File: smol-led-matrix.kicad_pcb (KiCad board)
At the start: 4 copper layers, 20.4 x 20.4 mm, 226 parts, among them U1 STM32L431CBTx

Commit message: Place parts
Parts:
- added C1: 100nF, Capacitor_SMD:C_0402_1005Metric, F.Cu at (131.6, 118.8)
- added C2: 100nF, Capacitor_SMD:C_0402_1005Metric, F.Cu at (124.8, 115.7)
- added C3: 100nF, Capacitor_SMD:C_0402_1005Metric, F.Cu at (144.2, 102.6)
- added C4: 1uF, Capacitor_SMD:C_0402_1005Metric, F.Cu at (139.3, 99.8)
- added C5: 100nF, Capacitor_SMD:C_0402_1005Metric, F.Cu at (129.8, 118.8)
- added C6: 1uF, Capacitor_SMD:C_0402_1005Metric, F.Cu at (138.8, 111.2)
- added C7: 1uF, Capacitor_SMD:C_0402_1005Metric, F.Cu at (140.5, 111.2)
- added C8: 100nF, Capacitor_SMD:C_0402_1005Metric, F.Cu at (126.1, 109.3)
- added C9: 100nF, Capacitor_SMD:C_0402_1005Metric, F.Cu at (134.3, 109.3)
- added D226: 1N4148, Diode_SMD:D_SOD-323F, F.Cu at (140.3, 101.9)
- added D227: LED, LED_SMD:LED_0402_1005Metric, F.Cu at (140.8, 99.6)
- added J1: USB_C_Receptacle_USB2.0, Connector_USB:USB_C_Receptacle_Palconn_UTC16-G, F.Cu at (129.4, 103.2)
- added J2: TagConnect_TC2030_SWD, Connector:Tag-Connect_TC2030-IDC-NL_2x03_P1.27mm_Vertical, F.Cu at (137.7, 117.3)
- added Q1: FS8205, Package_TO_SOT_SMD:SOT-23-6, F.Cu at (139.2, 105.3)
- added Q2: AO3401A, Package_TO_SOT_SMD:SOT-23, F.Cu at (139.6, 108.8)
- added R1: 5.1kR, Resistor_SMD:R_0402_1005Metric, F.Cu at (131.2, 107.3)
- added R2: 5.1kR, Resistor_SMD:R_0402_1005Metric, F.Cu at (127.1, 107.3)
- added R3: 27kR, Resistor_SMD:R_0402_1005Metric, F.Cu at (134.9, 102.9)
- added R4: 27kR, Resistor_SMD:R_0402_1005Metric, F.Cu at (136.7, 102.8)
- added R5: 27kR, Resistor_SMD:R_0402_1005Metric, F.Cu at (143.5, 107.7)
- added RN1: 1kR, Resistor_SMD:R_Array_Concave_4x0402, F.Cu at (136.2, 113.4)
- added RN2: 1kR, Resistor_SMD:R_Array_Concave_4x0402, F.Cu at (142.5, 102.5)
- added RN3: 1kR, Resistor_SMD:R_Array_Concave_4x0402, F.Cu at (136.9, 108.4)
- added RN4: 1kR, Resistor_SMD:R_Array_Concave_4x0402, F.Cu at (136.9, 110.9)
- added RN5: 1kR, Resistor_SMD:R_Array_Concave_4x0402, F.Cu at (136.0, 105.9)
- added SW1: SW_Push, Button_Switch_SMD:SW_Push_SPST_NO_Alps_SKRK, F.Cu at (142.9, 111.1)
- added SW2: SW_Push, Button_Switch_SMD:SW_Push_SPST_NO_Alps_SKRK, F.Cu at (142.9, 116.5)
- added TP1: BAT+, TestPoint:TestPoint_Pad_2.0x2.0mm, F.Cu at (125.6, 118.0)
- added TP2: BAT-, TestPoint:TestPoint_Pad_2.0x2.0mm, F.Cu at (143.4, 100.2)
- added U2: DW01+G, Package_TO_SOT_SMD:SOT-23-6, F.Cu at (142.8, 105.3)
- added U3: TP4054, Package_TO_SOT_SMD:TSOT-23-5, F.Cu at (136.6, 100.6)
- added U4: XC6206P332MR, Package_TO_SOT_SMD:SOT-23, F.Cu at (139.5, 113.5)
- U1: value STM32L431CBTx -> STM32L433CBTx
- moved U1 4.60 mm to (130.2, 113.4), turned to 90 degrees
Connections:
- net Net-(U1-Pad28) renamed /K15
- U1 pad 18: Net-(U1-Pad18) -> /K0
- U1 pad 19: Net-(U1-Pad19) -> /K1
- U1 pad 20: Net-(U1-Pad20) -> /K2
- U1 pad 21: Net-(U1-Pad21) -> /K10
- U1 pad 22: Net-(U1-Pad22) -> /K11
- U1 pad 23: Net-(U1-Pad23) -> GND
- U1 pad 24: Net-(U1-Pad24) -> +3V3
- U1 pad 25: Net-(U1-Pad25) -> /K12
- U1 pad 26: Net-(U1-Pad26) -> /K13
- U1 pad 27: Net-(U1-Pad27) -> /K14
- U1 pad 32: Net-(U1-Pad32) -> /D-
- U1 pad 33: Net-(U1-Pad33) -> /D+
- U1 pad 35: Net-(U1-Pad35) -> GND
- U1 pad 36: Net-(U1-Pad36) -> +3V3
- U1 pad 39: Net-(U1-Pad39) -> /K3
- U1 pad 40: Net-(U1-Pad40) -> /K4
- U1 pad 41: Net-(U1-Pad41) -> /K5
- U1 pad 42: Net-(U1-Pad42) -> /K6
- U1 pad 43: Net-(U1-Pad43) -> /K7
- U1 pad 45: Net-(U1-Pad45) -> /K8
- U1 pad 46: Net-(U1-Pad46) -> /K9
- U1 pad 47: Net-(U1-Pad47) -> GND
- U1 pad 48: Net-(U1-Pad48) -> +3V3
- U1 pad 7: Net-(U1-Pad7) -> /~RST
- U1 pad 8: Net-(U1-Pad8) -> GND
- U1 pad 9: Net-(U1-Pad9) -> +3V3
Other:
- board size 20.4 x 20.4 mm -> 45.8 x 20.4 mm

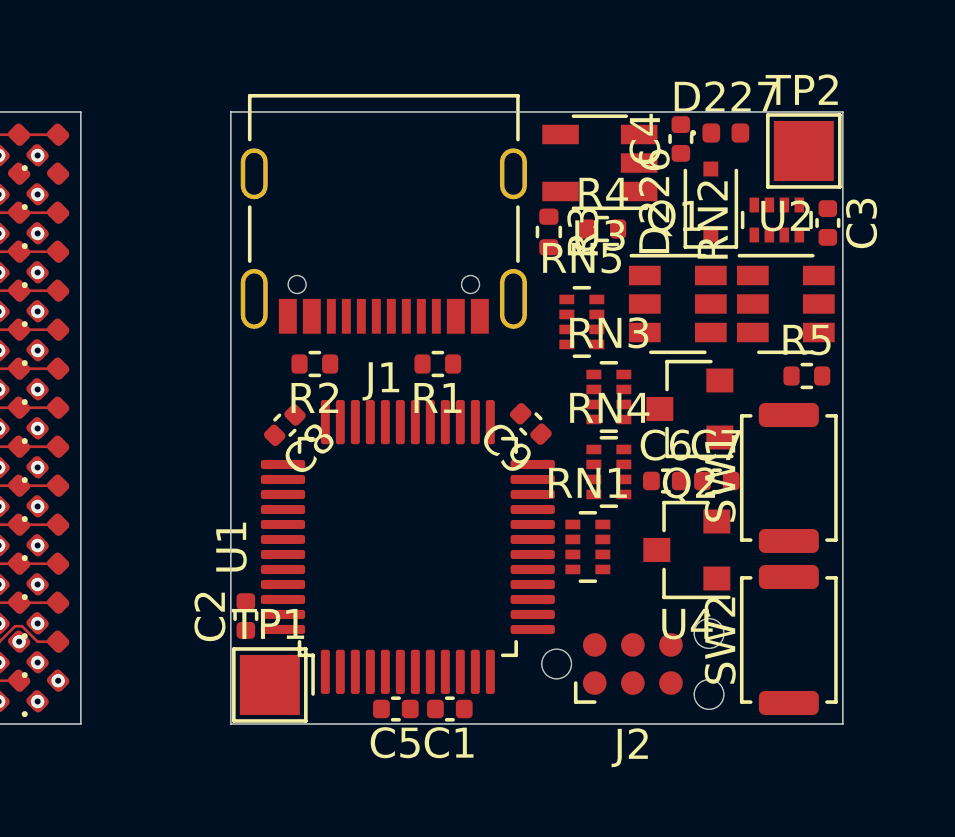
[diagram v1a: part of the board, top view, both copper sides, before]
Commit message: Hide designators
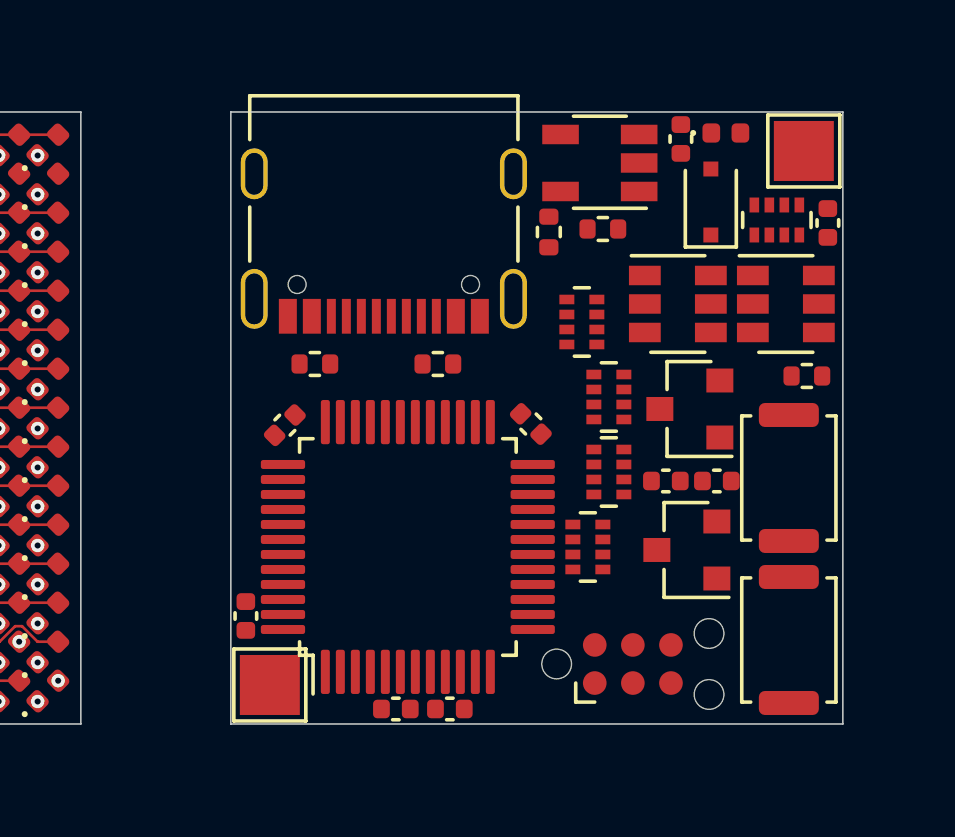
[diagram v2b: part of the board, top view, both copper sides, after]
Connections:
- net Net-(C3-Pad1) renamed /BAT-

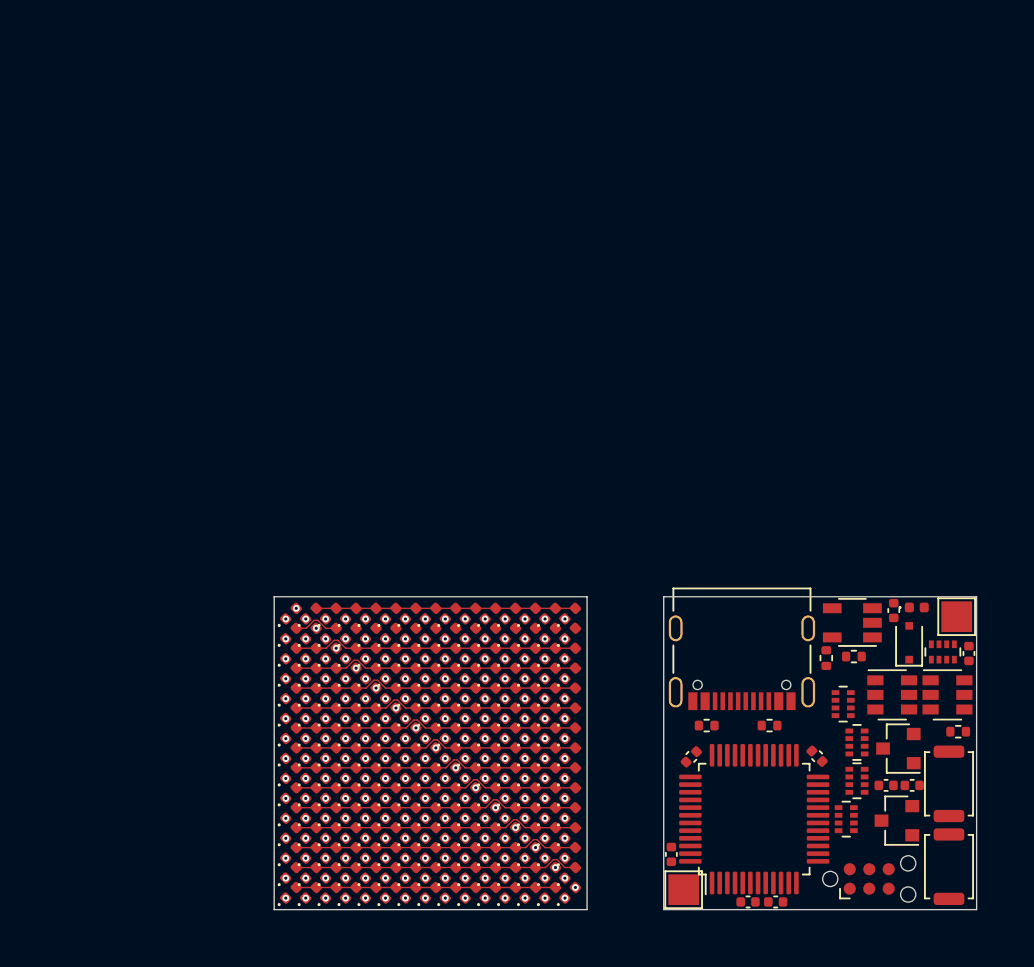
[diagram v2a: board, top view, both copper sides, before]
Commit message: Decide BGA ball placement
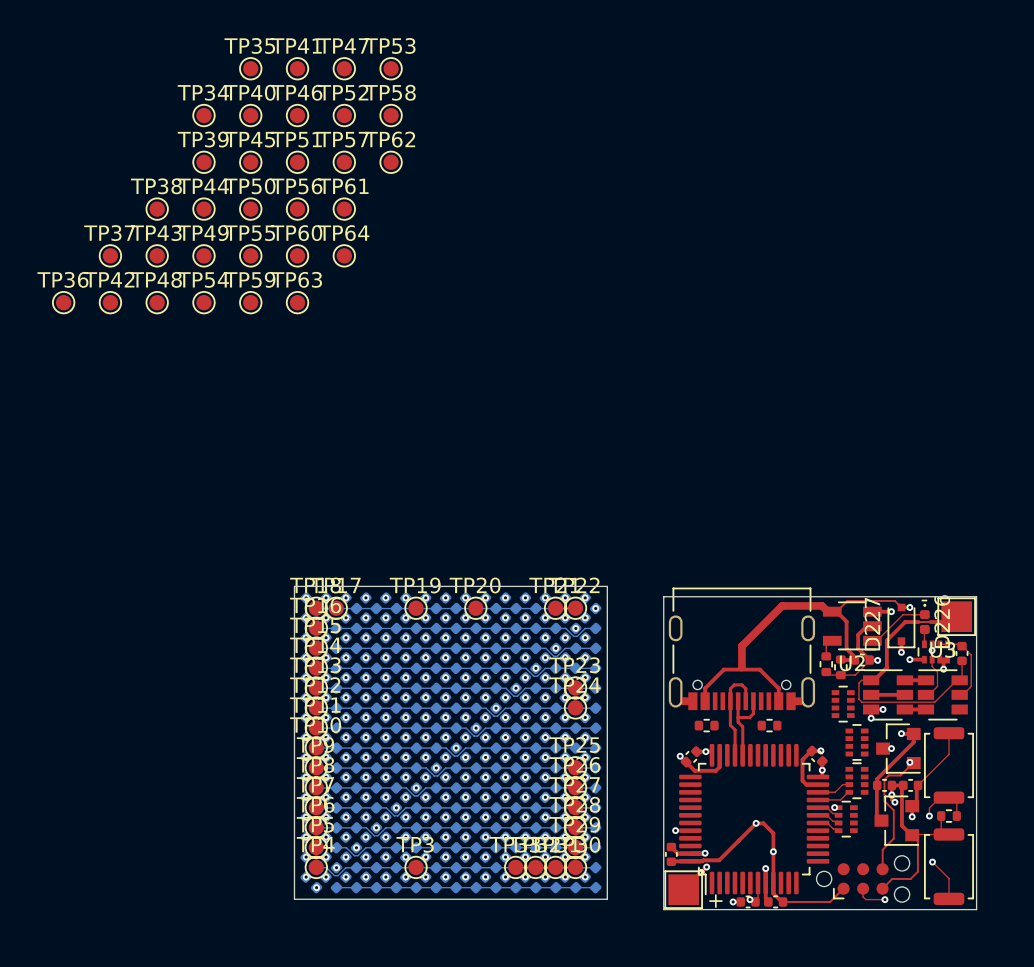
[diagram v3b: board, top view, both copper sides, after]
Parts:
- added TP10: TestPoint, TestPoint:TestPoint_Pad_D1.0mm, F.Cu at (101.7, 108.8)
- added TP11: TestPoint, TestPoint:TestPoint_Pad_D1.0mm, F.Cu at (101.7, 107.5)
- added TP12: TestPoint, TestPoint:TestPoint_Pad_D1.0mm, F.Cu at (101.7, 106.2)
- added TP13: TestPoint, TestPoint:TestPoint_Pad_D1.0mm, F.Cu at (101.7, 104.8)
- added TP14: TestPoint, TestPoint:TestPoint_Pad_D1.0mm, F.Cu at (101.7, 103.5)
- added TP15: TestPoint, TestPoint:TestPoint_Pad_D1.0mm, F.Cu at (101.7, 102.2)
- added TP16: TestPoint, TestPoint:TestPoint_Pad_D1.0mm, F.Cu at (101.7, 101.0)
- added TP17: TestPoint, TestPoint:TestPoint_Pad_D1.0mm, F.Cu at (103.0, 99.7)
- added TP18: TestPoint, TestPoint:TestPoint_Pad_D1.0mm, F.Cu at (101.7, 99.7)
- added TP19: TestPoint, TestPoint:TestPoint_Pad_D1.0mm, F.Cu at (108.2, 99.7)
- added TP20: TestPoint, TestPoint:TestPoint_Pad_D1.0mm, F.Cu at (112.0, 99.7)
- added TP21: TestPoint, TestPoint:TestPoint_Pad_D1.0mm, F.Cu at (117.2, 99.7)
- added TP22: TestPoint, TestPoint:TestPoint_Pad_D1.0mm, F.Cu at (118.5, 99.7)
- added TP23: TestPoint, TestPoint:TestPoint_Pad_D1.0mm, F.Cu at (118.5, 104.8)
- added TP24: TestPoint, TestPoint:TestPoint_Pad_D1.0mm, F.Cu at (118.5, 106.2)
- added TP25: TestPoint, TestPoint:TestPoint_Pad_D1.0mm, F.Cu at (118.5, 110.0)
- added TP26: TestPoint, TestPoint:TestPoint_Pad_D1.0mm, F.Cu at (118.5, 111.3)
- added TP27: TestPoint, TestPoint:TestPoint_Pad_D1.0mm, F.Cu at (118.5, 112.7)
- added TP28: TestPoint, TestPoint:TestPoint_Pad_D1.0mm, F.Cu at (118.5, 114.0)
- added TP29: TestPoint, TestPoint:TestPoint_Pad_D1.0mm, F.Cu at (118.5, 115.2)
- added TP3: TestPoint, TestPoint:TestPoint_Pad_D1.0mm, F.Cu at (108.2, 116.5)
- added TP30: TestPoint, TestPoint:TestPoint_Pad_D1.0mm, F.Cu at (118.5, 116.5)
- added TP31: TestPoint, TestPoint:TestPoint_Pad_D1.0mm, F.Cu at (117.2, 116.5)
- added TP32: TestPoint, TestPoint:TestPoint_Pad_D1.0mm, F.Cu at (116.0, 116.5)
- added TP33: TestPoint, TestPoint:TestPoint_Pad_D1.0mm, F.Cu at (114.7, 116.5)
- added TP34: TestPoint, TestPoint:TestPoint_Pad_D1.0mm, F.Cu at (94.3, 67.5)
- added TP35: TestPoint, TestPoint:TestPoint_Pad_D1.0mm, F.Cu at (97.4, 64.5)
- added TP36: TestPoint, TestPoint:TestPoint_Pad_D1.0mm, F.Cu at (85.2, 79.7)
- added TP37: TestPoint, TestPoint:TestPoint_Pad_D1.0mm, F.Cu at (88.2, 76.7)
- added TP38: TestPoint, TestPoint:TestPoint_Pad_D1.0mm, F.Cu at (91.3, 73.6)
- added TP39: TestPoint, TestPoint:TestPoint_Pad_D1.0mm, F.Cu at (94.3, 70.6)
- added TP4: TestPoint, TestPoint:TestPoint_Pad_D1.0mm, F.Cu at (101.7, 116.5)
- added TP40: TestPoint, TestPoint:TestPoint_Pad_D1.0mm, F.Cu at (97.4, 67.5)
- added TP41: TestPoint, TestPoint:TestPoint_Pad_D1.0mm, F.Cu at (100.4, 64.5)
- added TP42: TestPoint, TestPoint:TestPoint_Pad_D1.0mm, F.Cu at (88.2, 79.7)
- added TP43: TestPoint, TestPoint:TestPoint_Pad_D1.0mm, F.Cu at (91.3, 76.7)
- added TP44: TestPoint, TestPoint:TestPoint_Pad_D1.0mm, F.Cu at (94.3, 73.6)
- added TP45: TestPoint, TestPoint:TestPoint_Pad_D1.0mm, F.Cu at (97.4, 70.6)
- added TP46: TestPoint, TestPoint:TestPoint_Pad_D1.0mm, F.Cu at (100.4, 67.5)
- added TP47: TestPoint, TestPoint:TestPoint_Pad_D1.0mm, F.Cu at (103.5, 64.5)
- added TP48: TestPoint, TestPoint:TestPoint_Pad_D1.0mm, F.Cu at (91.3, 79.7)
- added TP49: TestPoint, TestPoint:TestPoint_Pad_D1.0mm, F.Cu at (94.3, 76.7)
- added TP5: TestPoint, TestPoint:TestPoint_Pad_D1.0mm, F.Cu at (101.7, 115.2)
- added TP50: TestPoint, TestPoint:TestPoint_Pad_D1.0mm, F.Cu at (97.4, 73.6)
- added TP51: TestPoint, TestPoint:TestPoint_Pad_D1.0mm, F.Cu at (100.4, 70.6)
- added TP52: TestPoint, TestPoint:TestPoint_Pad_D1.0mm, F.Cu at (103.5, 67.5)
- added TP53: TestPoint, TestPoint:TestPoint_Pad_D1.0mm, F.Cu at (106.5, 64.5)
- added TP54: TestPoint, TestPoint:TestPoint_Pad_D1.0mm, F.Cu at (94.3, 79.7)
- added TP55: TestPoint, TestPoint:TestPoint_Pad_D1.0mm, F.Cu at (97.4, 76.7)
- added TP56: TestPoint, TestPoint:TestPoint_Pad_D1.0mm, F.Cu at (100.4, 73.6)
- added TP57: TestPoint, TestPoint:TestPoint_Pad_D1.0mm, F.Cu at (103.5, 70.6)
- added TP58: TestPoint, TestPoint:TestPoint_Pad_D1.0mm, F.Cu at (106.5, 67.5)
- added TP59: TestPoint, TestPoint:TestPoint_Pad_D1.0mm, F.Cu at (97.4, 79.7)
- added TP6: TestPoint, TestPoint:TestPoint_Pad_D1.0mm, F.Cu at (101.7, 114.0)
- added TP60: TestPoint, TestPoint:TestPoint_Pad_D1.0mm, F.Cu at (100.4, 76.7)
- added TP61: TestPoint, TestPoint:TestPoint_Pad_D1.0mm, F.Cu at (103.5, 73.6)
- added TP62: TestPoint, TestPoint:TestPoint_Pad_D1.0mm, F.Cu at (106.5, 70.6)
- added TP63: TestPoint, TestPoint:TestPoint_Pad_D1.0mm, F.Cu at (100.4, 79.7)
- added TP64: TestPoint, TestPoint:TestPoint_Pad_D1.0mm, F.Cu at (103.5, 76.7)
- added TP7: TestPoint, TestPoint:TestPoint_Pad_D1.0mm, F.Cu at (101.7, 112.7)
- added TP8: TestPoint, TestPoint:TestPoint_Pad_D1.0mm, F.Cu at (101.7, 111.3)
- added TP9: TestPoint, TestPoint:TestPoint_Pad_D1.0mm, F.Cu at (101.7, 110.0)
- C3: value 100nF -> 1uF
- C4: value 1uF -> 100nF
- D1, D10, D100, D101, D102, D103, D104, D105, D106, D107, D108, D109, D11, D110, D111, D112, D113, D114, D115, D116, D117, D118, D119, D12, D120, D121, D122, D123, D124, D125, D126, D127, D128, D129, D13, D130, D131, D132, D133, D134, D135, D136, D137, D138, D139, D14, D140, D141, D142, D143, D144, D145, D146, D147, D148, D149, D15, D150, D151, D152, D153, D154, D155, D156, D157, D158, D159, D16, D160, D161, D162, D163, D164, D165, D166, D167, D168, D169, D17, D170, D171, D172, D173, D174, D175, D176, D177, D178, D179, D18, D180, D181, D182, D183, D184, D185, D186, D187, D188, D189, D19, D190, D191, D192, D193, D194, D195, D196, D197, D198, D199, D2, D20, D200, D201, D202, D203, D204, D205, D206, D207, D208, D209, D21, D210, D211, D212, D213, D214, D215, D216, D217, D218, D219, D22, D220, D221, D222, D223, D224, D225, D23, D24, D25, D26, D27, D28, D29, D3, D30, D31, D32, D33, D34, D35, D36, D37, D38, D39, D4, D40, D41, D42, D43, D44, D45, D46, D47, D48, D49, D5, D50, D51, D52, D53, D54, D55, D56, D57, D58, D59, D6, D60, D61, D62, D63, D64, D65, D66, D67, D68, D69, D7, D70, D71, D72, D73, D74, D75, D76, D77, D78, D79, D8, D80, D81, D82, D83, D84, D85, D86, D87, D88, D89, D9, D90, D91, D92, D93, D94, D95, D96, D97, D98, D99: moved to B.Cu
- D226: value 1N4148 -> LED; footprint Diode_SMD:D_SOD-323F -> LED_SMD:LED_0402_1005Metric
- D227: value LED -> 1N4148; footprint LED_SMD:LED_0402_1005Metric -> Diode_SMD:D_SOD-323F
- R1, R2: value 5.1kR -> 27kR
- R3, R4: value 27kR -> 5.1kR
- TP1: value BAT+ -> BAT-
- TP2: value BAT- -> BAT+
- U2: value DW01+G -> TP4054; footprint Package_TO_SOT_SMD:SOT-23-6 -> Package_TO_SOT_SMD:TSOT-23-5
- U3: value TP4054 -> DW01+G; footprint Package_TO_SOT_SMD:TSOT-23-5 -> Package_TO_SOT_SMD:SOT-23-6
- moved TP1 25.2 mm to (143.4, 100.2)
- moved TP2 25.2 mm to (125.6, 118.0)
- moved D105 18.9 mm to (109.1, 99.3), turned to 315 degrees
- moved D120 18.9 mm to (110.4, 99.3), turned to 315 degrees
- moved D135 18.9 mm to (111.7, 99.3), turned to 315 degrees
- moved D15 18.9 mm to (101.3, 99.3), turned to 315 degrees
- moved D150 18.9 mm to (113.0, 99.3), turned to 315 degrees
- moved D165 18.9 mm to (114.3, 99.3), turned to 315 degrees
- moved D180 18.9 mm to (115.6, 99.3), turned to 315 degrees
- moved D195 18.9 mm to (116.9, 99.3), turned to 315 degrees
- moved D210 18.9 mm to (118.2, 99.3), turned to 315 degrees
- moved D225 18.9 mm to (119.5, 99.3), turned to 315 degrees
- moved D30 18.9 mm to (102.6, 99.3), turned to 315 degrees
- moved D45 18.9 mm to (103.9, 99.3), turned to 315 degrees
- moved D60 18.9 mm to (105.2, 99.3), turned to 315 degrees
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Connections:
- C3 pad 1: /BAT- -> GND
- C3 pad 2: Net-(C3-Pad2) -> +5V
- C4 pad 1: GND -> /Power/BAT-
- C4 pad 2: +5V -> Net-(C4-Pad2)
- D226 pad 1: Net-(C6-Pad1) -> Net-(D226-Pad1)
- D226 pad 2: +5V -> /Power/CHG_LED+
- D227 pad 1: Net-(D227-Pad1) -> Net-(C6-Pad1)
- D227 pad 2: /CHG_LED+ -> +5V
- Q1 pad 1: /BAT- -> /Power/BAT-
- R1 pad 1: GND -> Net-(R1-Pad1)
- R1 pad 2: Net-(J1-PadA5) -> GND
- R2 pad 1: Net-(J1-PadB5) -> +5V
- R3 pad 1: Net-(R3-Pad1) -> GND
- R3 pad 2: GND -> Net-(J1-PadA5)
- R4 pad 1: +5V -> Net-(J1-PadB5)
- RN2 pad 2: GND -> Net-(RN2-Pad2)
- RN2 pad 5: Net-(C3-Pad2) -> Net-(C4-Pad2)
- RN2 pad 6: Net-(C3-Pad2) -> Net-(C4-Pad2)
- RN2 pad 7: Net-(RN2-Pad7) -> GND
- RN2 pad 8: /CHG_LED+ -> /Power/CHG_LED+
- RN4 pad 3: /K10 -> /K11
- RN4 pad 4: /K11 -> /K10
- RN4 pad 5: /A11 -> /A10
- RN4 pad 6: /A10 -> /A11
- TP1 pad 1: +BATT -> /Power/BAT-
- TP2 pad 1: /BAT- -> +BATT
- U2 pad 1: Net-(Q1-Pad6) -> Net-(D226-Pad1)
- U2 pad 2: Net-(RN2-Pad7) -> GND
- U2 pad 3: Net-(Q1-Pad4) -> +BATT
- U2 pad 4: Net-(U2-Pad4) -> +5V
- U2 pad 5: Net-(C3-Pad2) -> Net-(R1-Pad1)
- U3 pad 1: Net-(D227-Pad1) -> Net-(Q1-Pad6)
- U3 pad 2: GND -> Net-(RN2-Pad2)
- U3 pad 3: +BATT -> Net-(Q1-Pad4)
- U3 pad 4: +5V -> Net-(U3-Pad4)
- U3 pad 5: Net-(R3-Pad1) -> Net-(C4-Pad2)
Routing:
- net +3V3: track 0.00 -> 46.9 mm, vias 0 -> 5
- net +5V: track 0.00 -> 46.0 mm, vias 0 -> 3
- net +BATT: track 0.00 -> 42.0 mm, vias 0 -> 5
- net GND: track 0.00 -> 38.6 mm, vias 0 -> 11
- net Net-(R5-Pad2): track 0.00 -> 25.5 mm, vias 0 -> 2
- net /Power/BAT-: track 0.00 -> 21.4 mm
- net /~RST: track 0.00 -> 20.5 mm, vias 0 -> 3
- net /A1: track 3.03 -> 18.6 mm
- net Net-(C6-Pad1): track 0.00 -> 13.7 mm, vias 0 -> 2
- net /D+: track 0.00 -> 6.48 mm
- net /D-: track 0.00 -> 5.57 mm
- net Net-(C4-Pad2): track 0.00 -> 5.32 mm
- net Net-(D226-Pad1): track 0.00 -> 4.17 mm
- net Net-(RN2-Pad2): track 0.00 -> 2.87 mm
- net /K11: track 18.2 -> 20.4 mm
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- added copper zone on In1.Cu, net GND
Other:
- board size 45.8 x 20.4 mm -> 44.5 x 21.1 mm
- board text added: "+"
- board text added: "-"

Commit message: Layout half done
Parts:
- D1, D10, D100, D101, D102, D103, D104, D105, D106, D107, D108, D109, D11, D110, D111, D112, D113, D114, D115, D116, D117, D118, D119, D12, D120, D121, D122, D123, D124, D125, D126, D127, D128, D129, D13, D130, D131, D132, D133, D134, D135, D136, D137, D138, D139, D14, D140, D141, D142, D143, D144, D145, D146, D147, D148, D149, D15, D150, D151, D152, D153, D154, D155, D156, D157, D158, D159, D16, D160, D161, D162, D163, D164, D165, D166, D167, D168, D169, D17, D170, D171, D172, D173, D174, D175, D176, D177, D178, D179, D18, D180, D181, D182, D183, D184, D185, D186, D187, D188, D189, D19, D190, D191, D192, D193, D194, D195, D196, D197, D198, D199, D2, D20, D200, D201, D202, D203, D204, D205, D206, D207, D208, D209, D21, D210, D211, D212, D213, D214, D215, D216, D217, D218, D219, D22, D220, D221, D222, D223, D224, D225, D23, D24, D25, D26, D27, D28, D29, D3, D30, D31, D32, D33, D34, D35, D36, D37, D38, D39, D4, D40, D41, D42, D43, D44, D45, D46, D47, D48, D49, D5, D50, D51, D52, D53, D54, D55, D56, D57, D58, D59, D6, D60, D61, D62, D63, D64, D65, D66, D67, D68, D69, D7, D70, D71, D72, D73, D74, D75, D76, D77, D78, D79, D8, D80, D81, D82, D83, D84, D85, D86, D87, D88, D89, D9, D90, D91, D92, D93, D94, D95, D96, D97, D98, D99: moved to F.Cu
- TP10, TP11, TP12, TP13, TP14, TP15, TP16, TP17, TP18, TP19, TP20, TP21, TP22, TP23, TP24, TP25, TP26, TP27, TP28, TP29, TP3, TP30, TP31, TP32, TP33, TP34, TP35, TP36, TP37, TP38, TP39, TP4, TP40, TP41, TP42, TP43, TP44, TP45, TP46, TP47, TP48, TP49, TP5, TP50, TP51, TP52, TP53, TP54, TP55, TP56, TP57, TP58, TP59, TP6, TP60, TP61, TP62, TP63, TP64, TP7, TP8, TP9: moved to B.Cu
- moved TP47 65.3 mm to (144.6, 115.2)
- moved TP49 64.1 mm to (144.6, 116.5)
- moved TP46 64.0 mm to (144.6, 114.0)
- moved TP48 63.7 mm to (143.2, 116.5)
- moved TP42 63.4 mm to (144.6, 108.8)
- moved TP45 63.2 mm to (144.6, 112.7)
- moved TP36 63.1 mm to (144.6, 101.0)
- moved TP43 62.9 mm to (144.6, 110.0)
- moved TP44 62.8 mm to (144.6, 111.3)
- moved TP37 61.9 mm to (144.6, 102.2)
- moved TP41 61.6 mm to (144.6, 107.5)
- moved TP38 61.1 mm to (144.6, 103.5)
- moved TP40 61.0 mm to (144.6, 106.2)
- moved TP39 60.8 mm to (144.6, 104.8)
- moved TP50 59.1 mm to (138.1, 116.5)
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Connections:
- RN5 pad 1: /K12 -> /K15
- RN5 pad 2: /K13 -> /K14
- RN5 pad 3: /K14 -> /K13
- RN5 pad 4: Net-(RN5-Pad4) -> /K12
- RN5 pad 5: Net-(RN5-Pad5) -> /A12
- RN5 pad 6: /A14 -> /A13
- RN5 pad 7: /A13 -> /A14
- RN5 pad 8: /A12 -> /A15
- TP33 pad 1: /K15 -> /A15
- TP64 pad 1: /K15 -> /A15
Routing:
- net /K8: track 18.2 -> 54.3 mm, vias 15 -> 17
- net /K7: track 18.2 -> 53.4 mm, vias 15 -> 17
- net /K4: track 18.2 -> 51.6 mm, vias 15 -> 18
- net /K6: track 18.2 -> 48.7 mm, vias 15 -> 17
- net /K3: track 18.5 -> 48.7 mm, vias 16 -> 18
- net /K5: track 18.2 -> 46.4 mm, vias 15 -> 17
- net Net-(J2-Pad2): track 0.00 -> 24.5 mm, vias 0 -> 2
- net /K10: track 20.4 -> 43.6 mm, vias 15 -> 16
- net Net-(J2-Pad4): track 0.00 -> 22.0 mm, vias 0 -> 2
- net /K11: track 20.4 -> 37.9 mm, vias 15 -> 16
- net /K1: track 19.6 -> 35.9 mm, vias 15 -> 16
- net /K2: track 19.6 -> 35.7 mm, vias 15 -> 16
- net /K14: track 18.2 -> 34.2 mm, vias 15 -> 16
- net /K9: track 18.2 -> 33.6 mm, vias 15 -> 17
- net /K12: track 18.2 -> 33.5 mm, vias 15 -> 16
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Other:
- board size 44.5 x 21.1 mm -> 46.4 x 20.4 mm
